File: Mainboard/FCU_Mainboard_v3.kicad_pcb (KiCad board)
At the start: 2 copper layers, 250 x 100 mm, 135 parts, among them J1 R_OLED, J10 AP2, J11 AP1, J12 BootLoader, J14 ALT_OLED, J15 VSPEED_OLED, J16 R_FD, J17 R_LS, J18 R_CSTR, J19 R_WPT, J2 L_OLED, J20 R_VORD, J21 R_NDB, J22 R_ARPT, J23 LB_PULL, J24 LB_PUSH, J25 LB_hPa/inHg, J26 L_FD, J27 L_LS, J28 L_CSTR, J29 L_WPT, J3 SPD_OLED, J30 SPD/MACH, J31 HDG/TRK, J32 MET_ALT, J33 LVL_OFF, J34 S_PUSH, J35 HDG_ENC, J36 RB_ENC, J37 H_PUSH, J38 RB_PULL, J39 RB_hPa/inHg, J4 HDG_OLED, J40 L_VORD, J41 SPD_ENC, J42 ALT_ENC, J43 A_PUSH, J44 RB_PUSH, J45 A_1H_1K, J46 VS_ENC, J47 L_NDB, J48 VS_PUSH, J49 RVOR/ADF_1, J5 H_T_OLED, J50 RVOR/ADF_2, J51 R_MAP_MODE, J52 L_ARPT, J53 R_MAP_RANGE, J54 L_MAP_MODE, J55 L_MAP_RANGE, J56 LB_ENC, J57 LVOR/ADF_1, J58 LVOR/ADF_2, J6 APPR, J69 S_PULL, J7 EXPED, J70 H_PULL, J71 A_PULL, J72 VS_PULL, J8 LOC, J9 A/THR, P1 USB_B, SW1 SW_DIP_x03, U1 CD74HC4067M, U2 CD74HC4067M, U3 CD74HC4067M, U4 CD74HC4067M, U5 ATMega2560, U6 CH340G, U7 AMS1117-3.3

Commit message: Widen the mainboard to 270mm and place the supply selector
The 250mm board had no free rectangle left for the selector: counting
tracks and not just footprints, the largest gaps near the power section
were 14x12mm and 42x7mm, neither of which takes the screw terminal.

The board grows 20mm to the right, to (20,20)-(290,120). Nothing that
already existed moves except H3 and H7, which go from x 265 to x 285; the
other five mounting holes stay, so only two brass inserts move. The 100mm
depth is untouched. The ground zone follows the outline.

J13, C25, U8, C26, C27, R32, R33 and R34 go in the new strip as a column
at x 273..284, with 2.7 to 5mm between courtyards. J13 is rotated so its
wire entry faces the new right edge.

Net surgery: P1 pin 1 and R14 pin 1 change from +5V to VBUS, and the
thirteen tracks and one via that held P1.1 inside +5V are removed -- both
the path north to the y 105.72 spine and the bottom-layer branch that fed
the west group.

0 schematic parity issues. The 20 unconnected items are the new nets: the
GND ones clear on the first zone refill, the rest are for the autorouter.
Cutting P1.1 out of +5V splits that net into a west and an east island
which both now hang off U8 pin 7, and leaves the spine dangling at its
west end. The four silkscreen warnings and the three courtyard overlaps
were already there.

Co-Authored-By: Claude Opus 5 <noreply@anthropic.com>
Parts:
- added C25: 100nF, Capacitor_SMD:C_1206_3216Metric_Pad1.33x1.80mm_HandSolder, F.Cu at (275.0, 48.0)
- added C26: 100nF, Capacitor_SMD:C_1206_3216Metric_Pad1.33x1.80mm_HandSolder, F.Cu at (275.0, 63.0)
- added C27: 220uF, Capacitor_SMD:C_Elec_6.3x7.7, F.Cu at (277.0, 71.0)
- added J13: 5V from PSU, TerminalBlock_Phoenix:TerminalBlock_Phoenix_PT-1,5-2-5.0-H_1x02_P5.00mm_Horizontal, F.Cu at (278.0, 40.0)
- added R32: 100k, Resistor_SMD:R_1206_3216Metric_Pad1.30x1.75mm_HandSolder, F.Cu at (275.0, 79.0)
- added R33: 100k, Resistor_SMD:R_1206_3216Metric_Pad1.30x1.75mm_HandSolder, F.Cu at (275.0, 84.0)
- added R34: 620, Resistor_SMD:R_1206_3216Metric_Pad1.30x1.75mm_HandSolder, F.Cu at (275.0, 89.0)
- added U8: TPS2115A, Package_SO:TSSOP-8_4.4x3mm_P0.65mm, F.Cu at (277.0, 56.0)
- moved H3 20.0 mm to (285.0, 25.0)
- moved H7 20.0 mm to (285.0, 115.0)
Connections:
- P1 pad 1: +5V -> /Power Connectors/VBUS
- R14 pad 1: +5V -> /Power Connectors/VBUS
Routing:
- net +5V: track 282.6 -> 242.5 mm, vias 6 -> 5
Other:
- board size 250 x 100 mm -> 270 x 100 mm

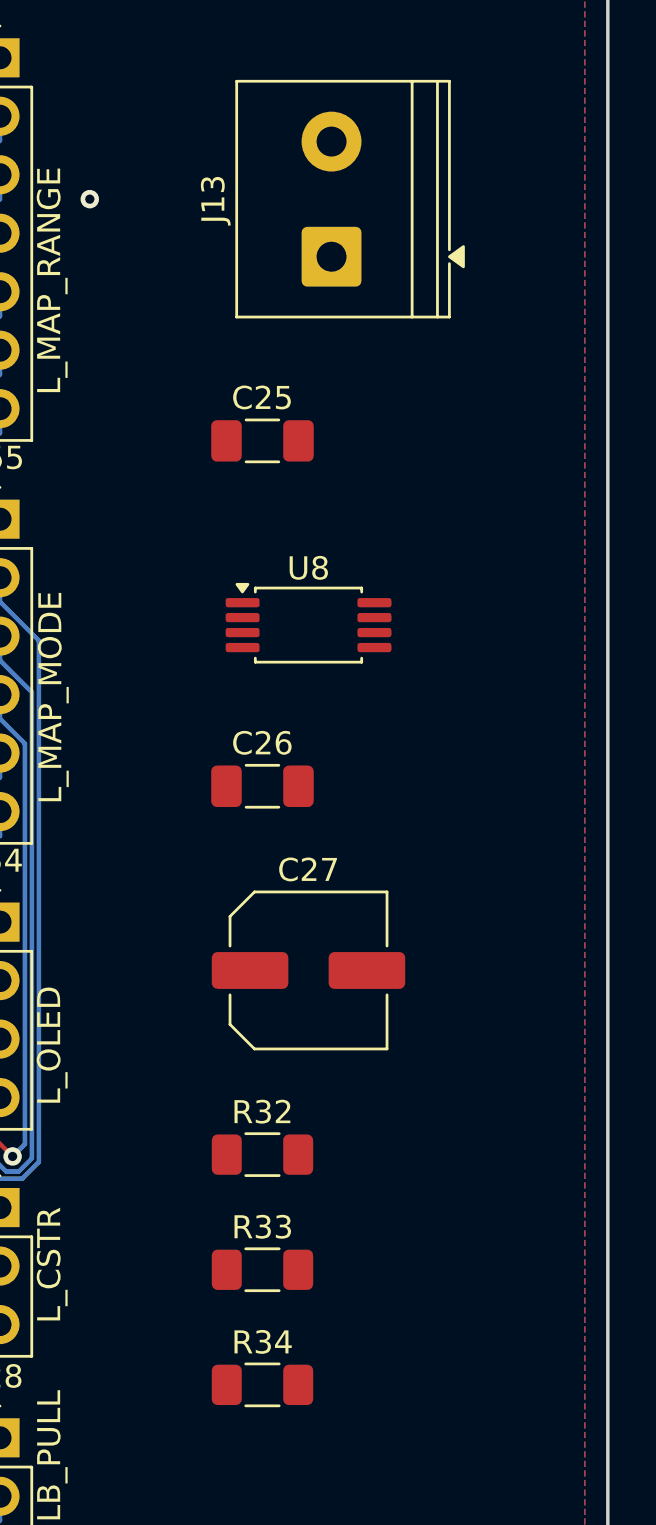
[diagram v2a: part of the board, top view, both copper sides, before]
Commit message: Route the selector cluster inside the mainboard's new strip
Everything local to the group is routed: 5V_EXT from J13 down the outer
channel to C25, U8 pin 8 and R32; +5V from pin 7 to C27; VBUS from pin 6 to
C26; the divider; the current-limit resistor; and the two ground pins to
their stitching vias.

The TSSOP pads are 1.475 x 0.4 on a 0.65 pitch, which leaves 0.25mm between
neighbours -- too little for a track -- so each pad escapes outward on its
own y and the tracks separate further out. Three channels on the right
(VBUS 282.0, +5V 283.5, 5V_EXT 285.5) and two on the left (SEL 271.7,
ILIM 270.5).

R32 and C27 are turned round so the pad the channel has to reach is the one
facing it. The three resistors also change order, ILIM first then the
divider: SEL sits above ILIM on U8 but its target was the higher of the two,
so whichever way the channels were assigned the pair crossed. Reordering
removes the crossing instead of working around it.

0 schematic parity issues, no crossings, no clearance violations. What is
left is what the autorouter is for: VBUS from P1 across the board, and +5V
from U8 pin 7 to the west and east islands that net split into. The GND
pads and the five new vias close on the first zone refill.

Co-Authored-By: Claude Opus 5 <noreply@anthropic.com>
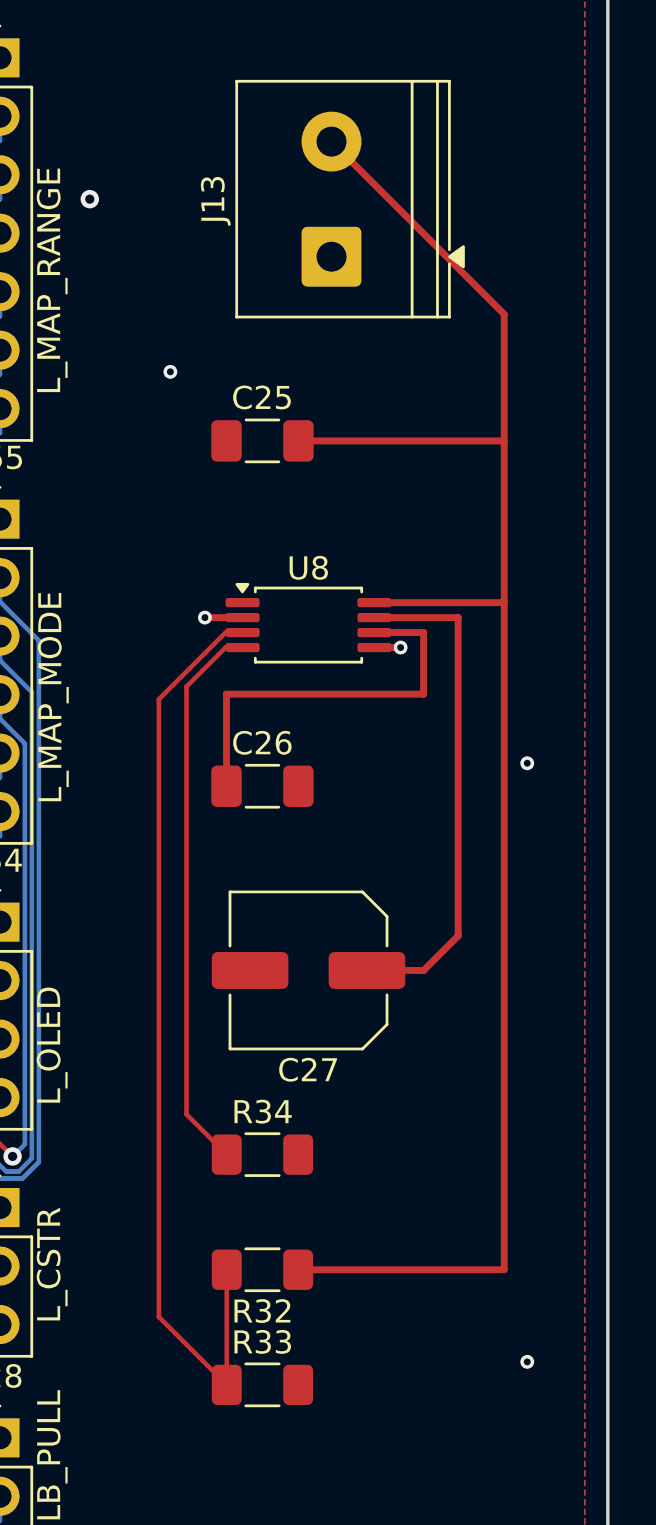
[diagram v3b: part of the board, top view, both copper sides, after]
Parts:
- moved R34 10.0 mm to (275.0, 79.0)
- moved R32 5.00 mm to (275.0, 84.0), turned to 180 degrees
- moved R33 5.00 mm to (275.0, 89.0)
- turned C27 to 180 degrees
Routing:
- net /Power Connectors/5V_EXT: track 0.00 -> 75.2 mm
- net /Power Connectors/SEL: track 0.00 -> 40.8 mm
- net Net-(U8-ILIM): track 0.00 -> 24.2 mm
- net +5V: track 242.5 -> 264.5 mm
- net /Power Connectors/VBUS: track 0.00 -> 17.4 mm
- net GND: track 94.0 -> 96.8 mm, vias 209 -> 214
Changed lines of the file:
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@@
 	(footprint "Capacitor_SMD:C_Elec_6.3x7.7"
 		(layer "F.Cu")
-		(at 277 71)
+		(at 277 71 180)
 		(descr "SMD capacitor, aluminum electrolytic nonpolar, 6.3x7.7mm")
 		(tags "capacitor electrolytic nonpolar")
 		(property "Reference" "C27"
-			(at 0 -4.35 0)
+			(at 0 -4.35 180)
 			(layer "F.SilkS")
 			(effects
@@
 		)
 		(property "Value" "220uF"
-			(at 0 4.35 0)
+			(at 0 4.35 180)
 			(layer "F.Fab")
 			(effects
@@
 		)
 		(property "Datasheet" ""
-			(at 0 0 0)
+			(at 0 0 180)
 			(unlocked yes)
 			(layer "F.Fab")
@@
 		)
 		(property "Description" "Polarized capacitor"
-			(at 0 0 0)
+			(at 0 0 180)
 			(unlocked yes)
 			(layer "F.Fab")
@@
 		)
 		(property "KiLib_Generator" "capacitor/SMD/elec_round"
-			(at 0 0 0)
+			(at 0 0 180)
 			(layer "F.SilkS")
 			(hide yes)
@@
 		)
 		(fp_text user "${REFERENCE}"
-			(at 0 0 0)
+			(at 0 0 180)
 			(layer "F.Fab")
 			(effects
@@
 		)
 		(pad "1" smd roundrect
-			(at -2.5375 0)
+			(at -2.5375 0 180)
 			(size 3.325 1.6)
 			(layers "F.Cu" "F.Mask" "F.Paste")
@@
 		)
 		(pad "2" smd roundrect
-			(at 2.5375 0)
+			(at 2.5375 0 180)
 			(size 3.325 1.6)
 			(layers "F.Cu" "F.Mask" "F.Paste")
@@
 	(footprint "Resistor_SMD:R_1206_3216Metric_Pad1.30x1.75mm_HandSolder"
 		(layer "F.Cu")
-		(at 275 79)
+		(at 275 84 180)
 		(descr "Resistor SMD 1206 (3216 Metric), square (rectangular) end terminal, IPC-7351 nominal with elongated pad for handsoldering. (Body size source: IPC-SM-782 page 72, https://www.pcb-3d.com/wordpress/wp-content/uploads/ipc-sm-782a_amendment_1_and_2.pdf)")
 		(tags "resistor handsolder")
 		(property "Reference" "R32"
-			(at 0 -1.83 0)
+			(at 0 -1.83 180)
 			(layer "F.SilkS")
 			(effects
@@
 		)
 		(property "Value" "100k"
-			(at 0 1.83 0)
+			(at 0 1.83 180)
 			(layer "F.Fab")
 			(effects
@@
 		)
 		(property "Datasheet" ""
-			(at 0 0 0)
+			(at 0 0 180)
 			(unlocked yes)
 			(layer "F.Fab")
@@
 		)
 		(property "Description" "Resistor"
-			(at 0 0 0)
+			(at 0 0 180)
 			(unlocked yes)
 			(layer "F.Fab")
@@
 		)
 		(property "KiLib_Generator" "SMD_2terminal_chip_molded"
-			(at 0 0 0)
+			(at 0 0 180)
 			(layer "F.SilkS")
 			(hide yes)
@@
 		)
 		(fp_text user "${REFERENCE}"
-			(at 0 0 0)
+			(at 0 0 180)
 			(layer "F.Fab")
 			(effects
@@
 		)
 		(pad "1" smd roundrect
-			(at -1.55 0)
+			(at -1.55 0 180)
 			(size 1.3 1.75)
 			(layers "F.Cu" "F.Mask" "F.Paste")
@@
 		)
 		(pad "2" smd roundrect
-			(at 1.55 0)
+			(at 1.55 0 180)
 			(size 1.3 1.75)
 			(layers "F.Cu" "F.Mask" "F.Paste")
@@
 	(footprint "Resistor_SMD:R_1206_3216Metric_Pad1.30x1.75mm_HandSolder"
 		(layer "F.Cu")
-		(at 275 84)
+		(at 275 89)
 		(descr "Resistor SMD 1206 (3216 Metric), square (rectangular) end terminal, IPC-7351 nominal with elongated pad for handsoldering. (Body size source: IPC-SM-782 page 72, https://www.pcb-3d.com/wordpress/wp-content/uploads/ipc-sm-782a_amendment_1_and_2.pdf)")
 		(tags "resistor handsolder")
@@
 	(footprint "Resistor_SMD:R_1206_3216Metric_Pad1.30x1.75mm_HandSolder"
 		(layer "F.Cu")
-		(at 275 89)
+		(at 275 79)
 		(descr "Resistor SMD 1206 (3216 Metric), square (rectangular) end terminal, IPC-7351 nominal with elongated pad for handsoldering. (Body size source: IPC-SM-782 page 72, https://www.pcb-3d.com/wordpress/wp-content/uploads/ipc-sm-782a_amendment_1_and_2.pdf)")
 		(tags "resistor handsolder")
@@
 	)
 	(embedded_fonts no)
+	(segment
+		(start 278 35)
+		(end 285.5 42.5)
+		(width 0.3)
+		(layer "F.Cu")
+		(net "/Power Connectors/5V_EXT")
+	)
+	(segment
+		(start 285.5 42.5)
+		(end 285.5 84)
+		(width 0.3)
+		(layer "F.Cu")
+		(net "/Power Connectors/5V_EXT")
+	)
+	(segment
+		(start 285.5 84)
+		(end 276.55 84)
+		(width 0.3)
+		(layer "F.Cu")
+		(net "/Power Connectors/5V_EXT")
+	)
+	(segment
+		(start 285.5 48)
+		(end 277 48)
+		(width 0.3)
+		(layer "F.Cu")
+		(net "/Power Connectors/5V_EXT")
+	)
+	(segment
+		(start 279.8625 55.025)
+		(end 285.5 55.025)
+		(width 0.3)
+		(layer "F.Cu")
+		(net "/Power Connectors/5V_EXT")
+	)
+	(segment
+		(start 279.8625 55.675)
+		(end 283.5 55.675)
+		(width 0.3)
+		(layer "F.Cu")
+		(net "+5V")
+	)
+	(segment
+		(start 283.5 55.675)
+		(end 283.5 69.5)
+		(width 0.3)
+		(layer "F.Cu")
+		(net "+5V")
+	)
+	(segment
+		(start 283.5 69.5)
+		(end 282 71)
+		(width 0.3)
+		(layer "F.Cu")
+		(net "+5V")
+	)
+	(segment
+		(start 282 71)
+		(end 279.5375 71)
+		(width 0.3)
+		(layer "F.Cu")
+		(net "+5V")
+	)
+	(segment
+		(start 279.8625 56.325)
+		(end 282 56.325)
+		(width 0.3)
+		(layer "F.Cu")
+		(net "/Power Connectors/VBUS")
+	)
+	(segment
+		(start 282 56.325)
+		(end 282 59)
+		(width 0.3)
+		(layer "F.Cu")
+		(net "/Power Connectors/VBUS")
+	)
+	(segment
+		(start 282 59)
+		(end 273.4375 59)
+		(width 0.3)
+		(layer "F.Cu")
+		(net "/Power Connectors/VBUS")
+	)
+	(segment
+		(start 273.4375 59)
+		(end 273.4375 63)
+		(width 0.3)
+		(layer "F.Cu")
+		(net "/Power Connectors/VBUS")
+	)
+	(segment
+		(start 274.1375 56.325)
+		(end 273.4 56.325)
+		(width 0.2)
+		(layer "F.Cu")
+		(net "/Power Connectors/SEL")
+	)
+	(segment
+		(start 273.4 56.325)
+		(end 270.5 59.225)
+		(width 0.2)
+		(layer "F.Cu")
+		(net "/Power Connectors/SEL")
+	)
+	(segment
+		(start 270.5 59.225)
+		(end 270.5 86.05)
+		(width 0.2)
+		(layer "F.Cu")
+		(net "/Power Connectors/SEL")
+	)
+	(segment
+		(start 270.5 86.05)
+		(end 273.45 89)
+		(width 0.2)
+		(layer "F.Cu")
+		(net "/Power Connectors/SEL")
+	)
+	(segment
+		(start 273.45 84)
+		(end 273.45 89)
+		(width 0.2)
+		(layer "F.Cu")
+		(net "/Power Connectors/SEL")
+	)
+	(segment
+		(start 274.1375 56.975)
+		(end 273.4 56.975)
+		(width 0.2)
+		(layer "F.Cu")
+		(net "Net-(U8-ILIM)")
+	)
+	(segment
+		(start 273.4 56.975)
+		(end 271.7 58.675)
+		(width 0.2)
+		(layer "F.Cu")
+		(net "Net-(U8-ILIM)")
+	)
+	(segment
+		(start 271.7 58.675)
+		(end 271.7 77.25)
+		(width 0.2)
+		(layer "F.Cu")
+		(net "Net-(U8-ILIM)")
+	)
+	(segment
+		(start 271.7 77.25)
+		(end 273.45 79)
+		(width 0.2)
+		(layer "F.Cu")
+		(net "Net-(U8-ILIM)")
+	)
+	(segment
+		(start 274.1375 55.675)
+		(end 272.5 55.675)
+		(width 0.3)
+		(layer "F.Cu")
+		(net "GND")
+	)
+	(segment
+		(start 279.8625 56.975)
+		(end 281 56.975)
+		(width 0.3)
+		(layer "F.Cu")
+		(net "GND")
+	)
+	(via
+		(at 272.5 55.675)
+		(size 0.6)
+		(drill 0.3)
+		(layers "F.Cu" "B.Cu")
+		(net "GND")
+	)
+	(via
+		(at 281 56.975)
+		(size 0.6)
+		(drill 0.3)
+		(layers "F.Cu" "B.Cu")
+		(net "GND")
+	)
+	(via
+		(at 286.5 62)
+		(size 0.6)
+		(drill 0.3)
+		(layers "F.Cu" "B.Cu")
+		(net "GND")
+	)
+	(via
+		(at 286.5 88)
+		(size 0.6)
+		(drill 0.3)
+		(layers "F.Cu" "B.Cu")
+		(net "GND")
+	)
+	(via
+		(at 271 45)
+		(size 0.6)
+		(drill 0.3)
+		(layers "F.Cu" "B.Cu")
+		(net "GND")
+	)
 )

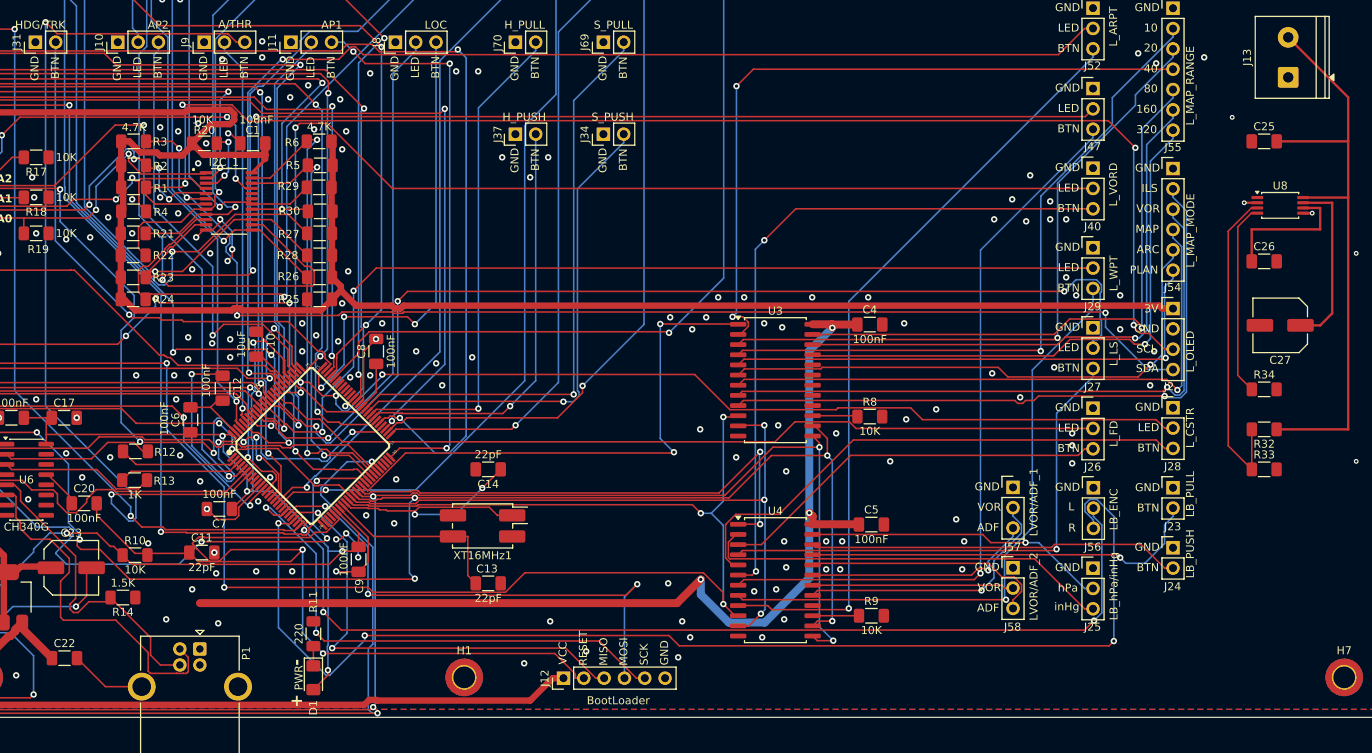
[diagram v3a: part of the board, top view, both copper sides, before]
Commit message: Close the +5V link between the board and the selector strip
The net was in two pieces: everything on the board in one, and U8 pin 7 with
C27 in the other, 53mm apart. The ratline for it starts at x 280, inside the
20mm added today, which is why it was easy to miss on screen.

Routed from C5 pin 1 at (224.34, 95.90) along the bottom edge to C27 pin 1.
The two vertical legs are on the back because the front is blocked at both
x 228 and x 279; the long horizontal stays on the front at y 118, so the
bottom plane takes two short slots instead of one 85mm one. Four vias.

Every leg was checked against all other-net copper before being written:
the tightest is 0.50mm, at C5's own ground pad, against a 0.1mm rule.

+5V is now a single connected component of 91 copper objects and 14 pads.
0 unconnected items, 0 schematic parity issues. The 17 clearance violations
and 1 isolated copper the file reports all name the stale pour; the four
silkscreen warnings were already there. Needs a refill.

Also includes the hand routing done in Pcbnew: VBUS from P1 to the strip,
the +5V west island back onto the spine, and work on ARPT_BTN, VORD_BTN,
MOSI, MP_S0 and MP_S2.

Co-Authored-By: Claude Opus 5 <noreply@anthropic.com>
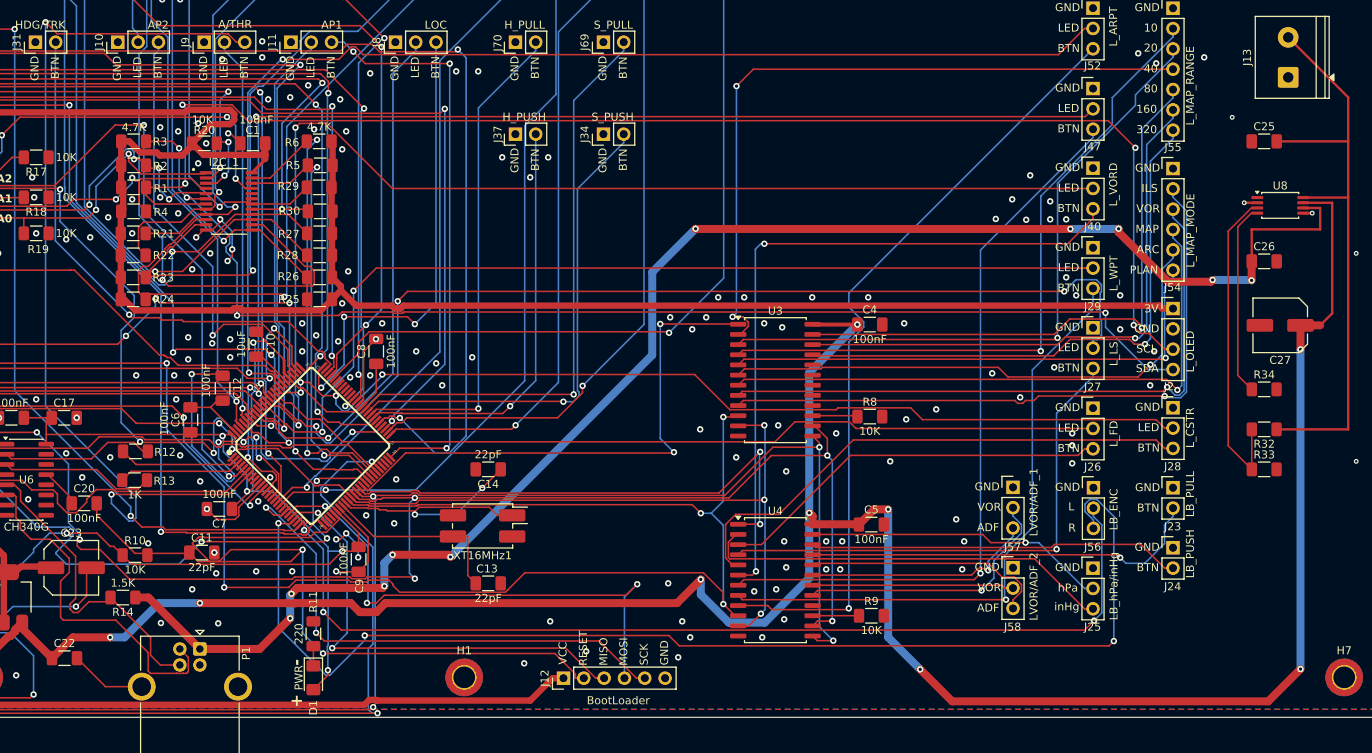
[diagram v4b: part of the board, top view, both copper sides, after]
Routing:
- net /Power Connectors/VBUS: track 17.4 -> 196.6 mm, vias 0 -> 10
- net +5V: track 264.5 -> 408.0 mm, vias 5 -> 11
- net MOSI: track 65.0 -> 66.6 mm
- net /EFIS_LEFT/ARPT_BTN: track 96.7 -> 98.2 mm
- net MP_S0: track 277.6 -> 278.7 mm
- net /EFIS_LEFT/VORD_BTN: track 87.0 -> 87.7 mm

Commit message: Anchor the last orphaned patch of ground
The board had one isolated_copper warning that KiCad pinned to the zone
origin instead of the island, so the whole outline lit up and there was no
way to see what it meant. The island is a 15.6 mm2 patch of front-side
ground down at x 125..135, y 102..111, fenced in by signal tracks with no
element of GND reaching into it.

A stitching via at (129, 106.6) drops it onto the back plane, which is the
one 9490 mm2 pour. The spot clears every other net by 0.55 mm on both
faces, well over the 0.2 mm the netclass asks for.

Also carries the hand routing and the silkscreen repositioning done in the
GUI. DRC: 0 violations, 0 unconnected, 0 parity.

Co-Authored-By: Claude Opus 5 <noreply@anthropic.com>
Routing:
- net GND: vias 214 -> 215
